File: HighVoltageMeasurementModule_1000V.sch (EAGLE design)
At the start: 8 parts

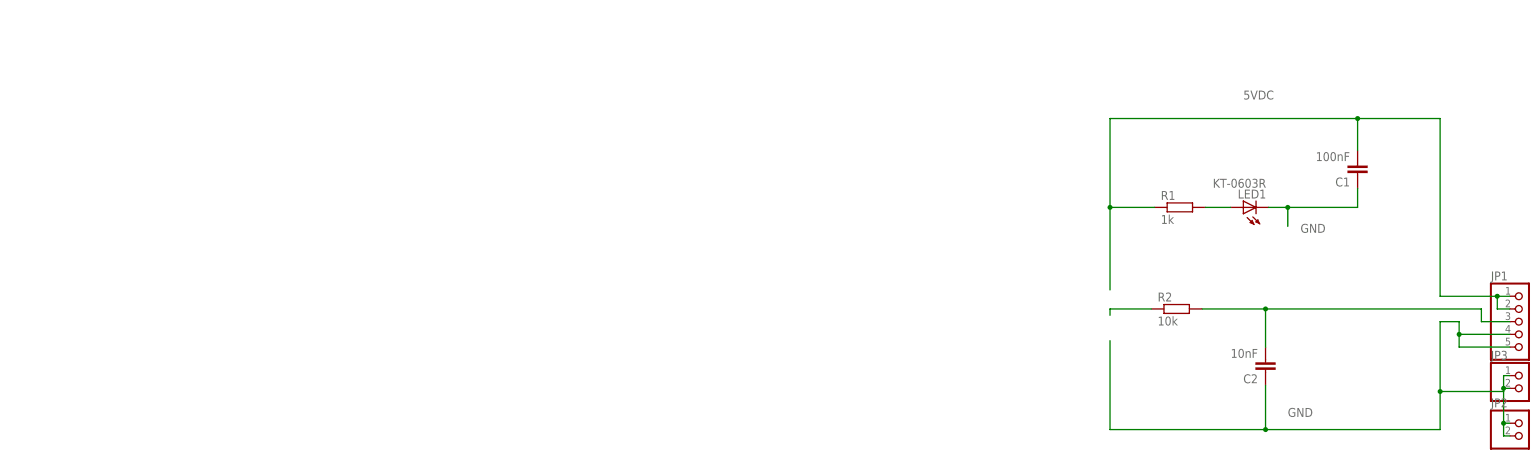
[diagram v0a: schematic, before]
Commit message: voltage module layouted
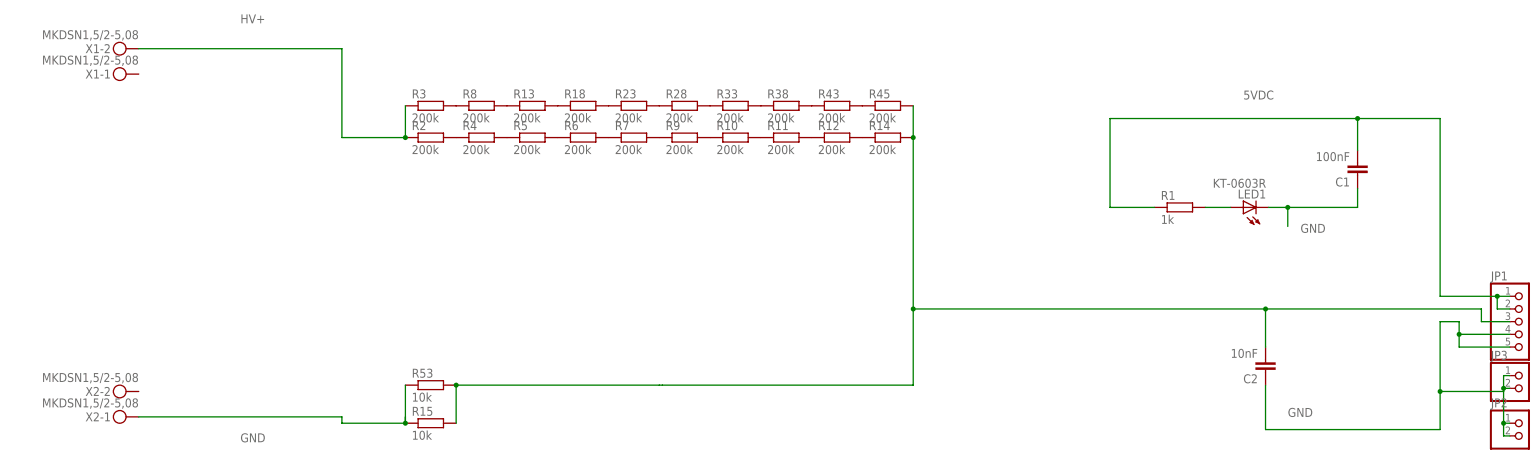
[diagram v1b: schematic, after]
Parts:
- added R10, R11, R12, R13, R14, R18, R23, R28, R3, R33, R38, R4, R43, R45, R5, R6, R7, R8, R9: 200k, rcl:R-EU_R0805
- added R15, R53: 10k, rcl:R-EU_R0805
- added X1, X2: MKDSN1,5/2-5,08, con-phoenix-508:MKDSN1,5/2-5,08
- R2: value 10k -> 200k
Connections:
- removed net N$6: C2.2, JP1.3, R2.2
- new net HV+: R2.1, R3.1, X1-2.KL
- new net N$10: R10.1, R9.2
- new net N$11: R10.2, R11.1
- new net N$12: R11.2, R12.1
- new net N$13: R12.2, R14.1
- new net N$14: R13.2, R18.1
- new net N$15: C2.2, JP1.3, R14.2, R15.2, R45.2, R53.2
- new net N$19: R18.2, R23.1
- new net N$2: R4.2, R5.1
- new net N$24: R23.2, R28.1
- new net N$29: R28.2, R33.1
- new net N$3: R5.2, R6.1
- new net N$34: R33.2, R38.1
- new net N$39: R38.2, R43.1
- new net N$4: R6.2, R7.1
- new net N$41: R43.2, R45.1
- new net N$7: R7.2, R9.1
- new net N$8: R3.2, R8.1
- new net N$9: R13.1, R8.2
- net GND: now also R15.1, R53.1, X2-1.KL
- net N$1: now also R2.2, R4.1; no longer R2.1
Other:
- moved on the sheet: R2
